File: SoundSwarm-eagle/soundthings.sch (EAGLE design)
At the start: 33 parts, among them Q2 IRLB8721PBF

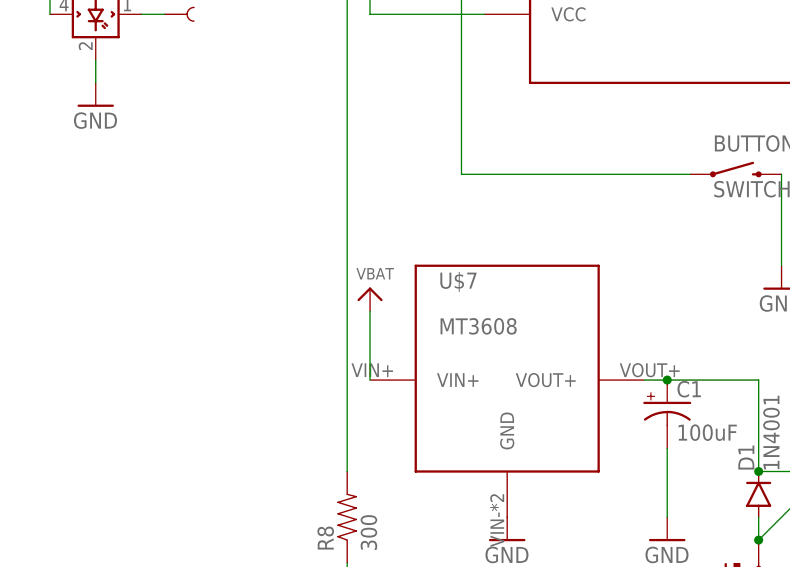
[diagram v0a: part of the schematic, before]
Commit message: Fixed: DC-DC on VDD (switched)
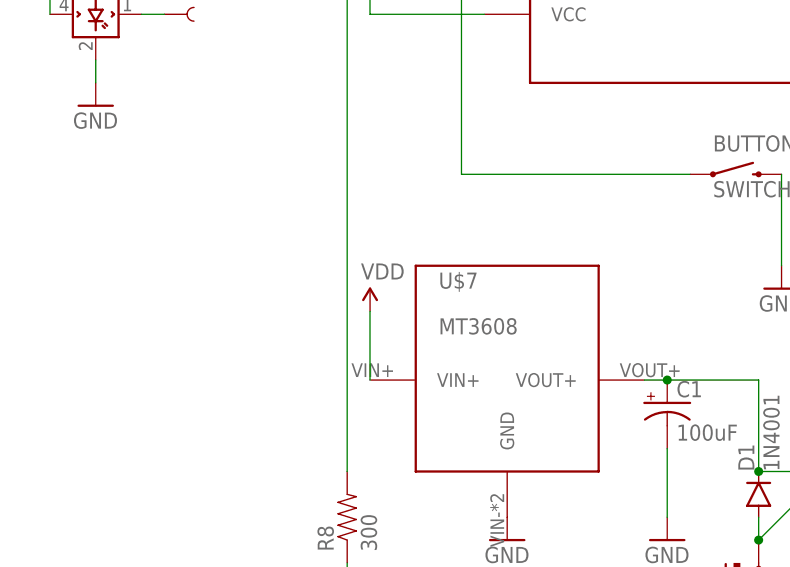
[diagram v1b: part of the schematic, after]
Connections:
- net VBAT: no longer U$7.VIN+
- net VDD: now also U$7.VIN+
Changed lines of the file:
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@@
 <part name="GND6" library="SparkFun-Aesthetics" deviceset="GND" device=""/>
 <part name="U$3" library="microbuilder" deviceset="VBAT" device=""/>
-<part name="U$4" library="microbuilder" deviceset="VBAT" device=""/>
 <part name="R8" library="SparkFun-Passives" deviceset="RESISTOR" device="AXIAL-0.3" value="300"/>
 <part name="U$5" library="lio" deviceset="TLV702" device="33"/>
@@
 <part name="GND" library="SparkFun-Passives" deviceset="TEST-POINT" device="TP_15TH_THRU"/>
 <part name="GND15" library="SparkFun-Aesthetics" deviceset="GND" device=""/>
+<part name="SUPPLY3" library="SparkFun-Aesthetics" deviceset="VDD" device=""/>
 </parts>
 <sheets>
@@
 <instance part="GND6" gate="1" x="124.46" y="162.56"/>
 <instance part="U$3" gate="G$1" x="45.72" y="157.48"/>
-<instance part="U$4" gate="G$1" x="27.94" y="53.34"/>
 <instance part="R8" gate="G$1" x="25.4" y="27.94" rot="R90"/>
 <instance part="U$5" gate="G$1" x="5.08" y="170.18"/>
@@
 </instance>
 <instance part="GND15" gate="1" x="93.98" y="137.16"/>
+<instance part="SUPPLY3" gate="VDD" x="27.94" y="50.8"/>
 </instances>
 <busses>
@@
 </segment>
 <segment>
-<pinref part="U$4" gate="G$1" pin="VBAT"/>
-<wire x1="27.94" y1="50.8" x2="27.94" y2="43.18" width="0.1524" layer="91"/>
-<pinref part="U$7" gate="G$1" pin="VIN+"/>
-</segment>
-<segment>
 <pinref part="R11" gate="G$1" pin="2"/>
 <pinref part="U$6" gate="G$1" pin="VBAT"/>
@@
 <wire x1="-2.54" y1="93.98" x2="-2.54" y2="88.9" width="0.1524" layer="91"/>
 </segment>
-</net>
+<segment>
+<wire x1="27.94" y1="50.8" x2="27.94" y2="43.18" width="0.1524" layer="91"/>
+<pinref part="U$7" gate="G$1" pin="VIN+"/>
+<pinref part="SUPPLY3" gate="VDD" pin="VDD"/>
+</segment>
+</net>

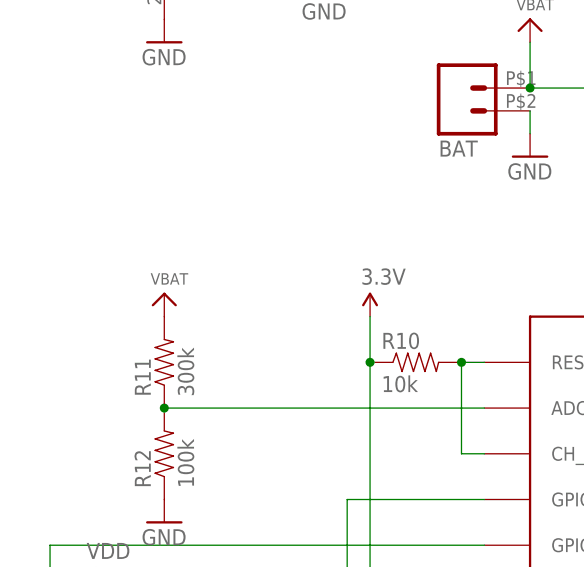
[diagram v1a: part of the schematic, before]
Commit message: SSv2c with fixed VDD battery measurement
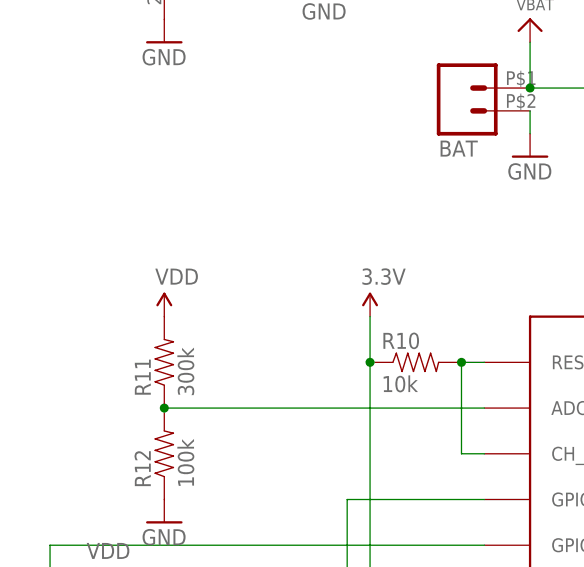
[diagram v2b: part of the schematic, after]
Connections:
- net VBAT: no longer R11.2
- net VDD: now also R11.2
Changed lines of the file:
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@@
 <part name="R11" library="SparkFun-Passives" deviceset="RESISTOR" device="AXIAL-0.3" value="300k"/>
 <part name="R12" library="SparkFun-Passives" deviceset="RESISTOR" device="AXIAL-0.3" value="100k"/>
-<part name="U$6" library="microbuilder" deviceset="VBAT" device=""/>
 <part name="GND11" library="SparkFun-Aesthetics" deviceset="GND" device=""/>
 <part name="SUPPLY1" library="SparkFun-Aesthetics" deviceset="5V" device=""/>
@@
 <part name="GND15" library="SparkFun-Aesthetics" deviceset="GND" device=""/>
 <part name="SUPPLY3" library="SparkFun-Aesthetics" deviceset="VDD" device=""/>
+<part name="SUPPLY10" library="SparkFun-Aesthetics" deviceset="VDD" device=""/>
 </parts>
 <sheets>
@@
 <instance part="R11" gate="G$1" x="5.08" y="119.38" rot="R90"/>
 <instance part="R12" gate="G$1" x="5.08" y="109.22" rot="R90"/>
-<instance part="U$6" gate="G$1" x="5.08" y="127"/>
 <instance part="GND11" gate="1" x="5.08" y="101.6"/>
 <instance part="SUPPLY1" gate="G$1" x="66.04" y="175.26"/>
@@
 <instance part="GND15" gate="1" x="93.98" y="137.16"/>
 <instance part="SUPPLY3" gate="VDD" x="27.94" y="50.8"/>
+<instance part="SUPPLY10" gate="VDD" x="5.08" y="124.46"/>
 </instances>
 <busses>
@@
 <wire x1="45.72" y1="149.86" x2="45.72" y2="154.94" width="0.1524" layer="91"/>
 </segment>
-<segment>
-<pinref part="R11" gate="G$1" pin="2"/>
-<pinref part="U$6" gate="G$1" pin="VBAT"/>
-</segment>
 </net>
 <net name="GPIO16" class="0">
@@
 <pinref part="SUPPLY3" gate="VDD" pin="VDD"/>
 </segment>
-</net>
+<segment>
+<pinref part="R11" gate="G$1" pin="2"/>
+<pinref part="SUPPLY10" gate="VDD" pin="VDD"/>
+</segment>
+</net>
